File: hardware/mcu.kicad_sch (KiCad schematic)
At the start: 19 parts, among them J1 Micro_SD_Card, SW8 BOOT, U1 ESP32-S3-WROOM-1, U10 PCA9555PW, U8 Ai-Thinker-Ra-02

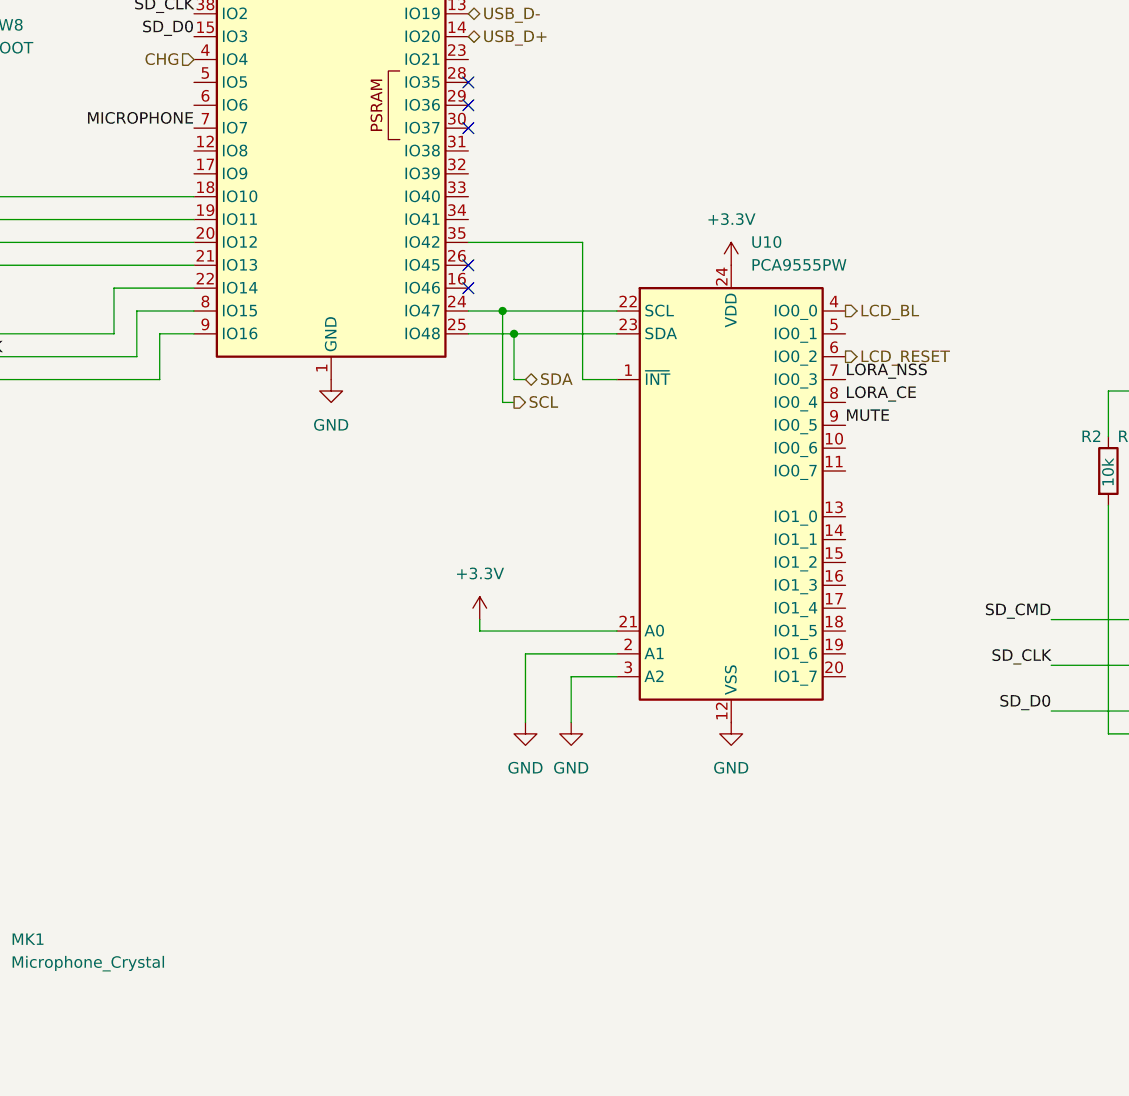
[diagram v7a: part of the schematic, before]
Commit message: Route I2C bus
Add decoupling capacitors to esp32 and io expandes
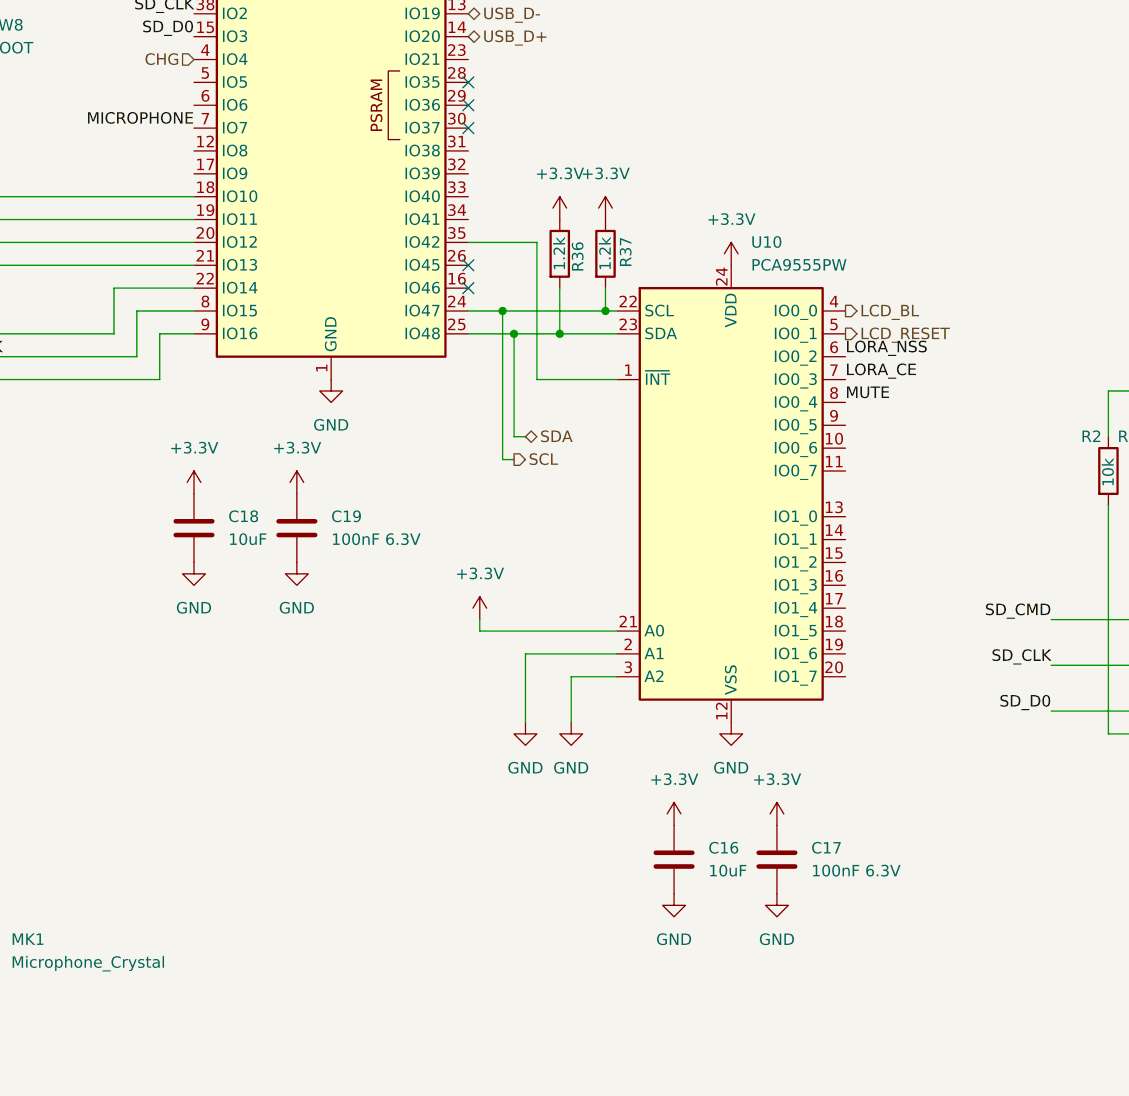
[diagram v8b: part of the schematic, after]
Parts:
- added C16, C18: 10uF, Capacitor_SMD:C_0603_1608Metric, symbol Device:C
- added C17, C19: 100nF 6.3V, Capacitor_SMD:C_0402_1005Metric, symbol Device:C
- added R36, R37: 1.2k, Resistor_SMD:R_0603_1608Metric, symbol Device:R
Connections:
- net +3.3V: now also C16.1, C17.1, C18.1, C19.1, R36.1, R37.1
- net GND: now also C16.2, C17.2, C18.2, C19.2
- net LCD_RESET: now also U10.5 (IO0_1); no longer U10.6 (IO0_2)
- net LORA_CE: now also U10.7 (IO0_3); no longer U10.8 (IO0_4)
- net LORA_NSS: now also U10.6 (IO0_2); no longer U10.7 (IO0_3)
- net MUTE: now also U10.8 (IO0_4); no longer U10.9 (IO0_5)
- net SCL: now also R37.2
- net SDA: now also R36.2
